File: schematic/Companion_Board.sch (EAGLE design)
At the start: 43 parts, among them J10 QSH-030-01-X-D-A, Q1 CSM-7X-DU

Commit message: Updated spec and schematic with pinheaders for reset and power.
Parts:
- added JP11: (no value), pinhead:PINHD-1X4/90
- added R12, R13: NC, resistor:R-US_R0805
- added TP4: TPPAD1-13, testpad:TPPAD1-13
- R7, R9: value ??k -> 270
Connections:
- net N$25 renamed FORCE_RESET
- net SBW_RST renamed SBW_TDIO
- removed net N$54: U$1.P1.4/UCA0STE/TCK/OA0+/A4
- removed net N$55: U$1.P1.5/UCA0CLK/TMS/TRI0O/A5
- new net N$25: R12.1, U$1.P1.4/UCA0STE/TCK/OA0+/A4
- new net N$34: R13.1, U$1.P1.5/UCA0CLK/TMS/TRI0O/A5
- new net N$48: J10.40, JP7.9
- net +3V3: now also TP4.TP
- net BSL_RXD: now also U$1.P1.7/UCA-TXD/UCA0SIMO/TB0.2/TDO/TRI0+/A7/VREF+; no longer U$1.P1.6/UCA0RXD/UCA0SOMI/TB0.1/TDI/TCLK/TRI0-/A6
- net BSL_TXD: now also U$1.P1.6/UCA0RXD/UCA0SOMI/TB0.1/TDI/TCLK/TRI0-/A6; no longer U$1.P1.7/UCA-TXD/UCA0SIMO/TB0.2/TDO/TRI0+/A7/VREF+
- net GND: now also JP11.2, JP11.4, R12.2, R13.2, TP1.TP
- net POWER_BTN_R: now also JP11.3
- net RESET_IN_R_L: now also JP11.1; no longer J10.40, JP7.9
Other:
- note added: "1-2: Board is internally powered (by Jetson), VCC_TARGET provides board voltage to debugger. 2-3: Board is powered by debugger."
- note added: "Grounding ADR sets I2C addr to 0x76 Connecting CS to VDDIO at power-up enables I2C interface."
- note added: "J10: Debug Connector Not populated"
- note added: "Reset_Switch Gnd Power_Switch Gnd"
- note added: "This is RXD/TXD from the perspective of the debugger."
- note removed: "Grounding ADR sets I2C addr to 0x76"
- note removed: "J10: Debug Connector"
- moved on the sheet: J10, JP6, JP7

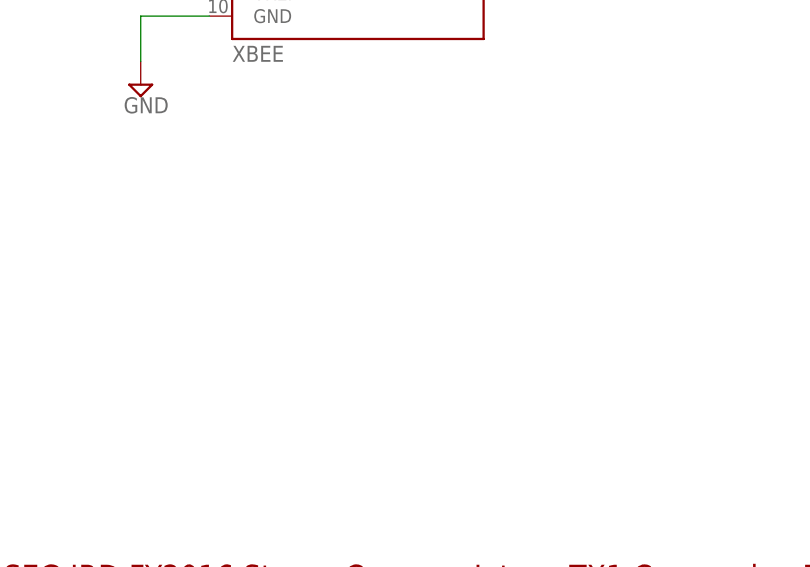
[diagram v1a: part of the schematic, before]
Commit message: Added mounting holes.
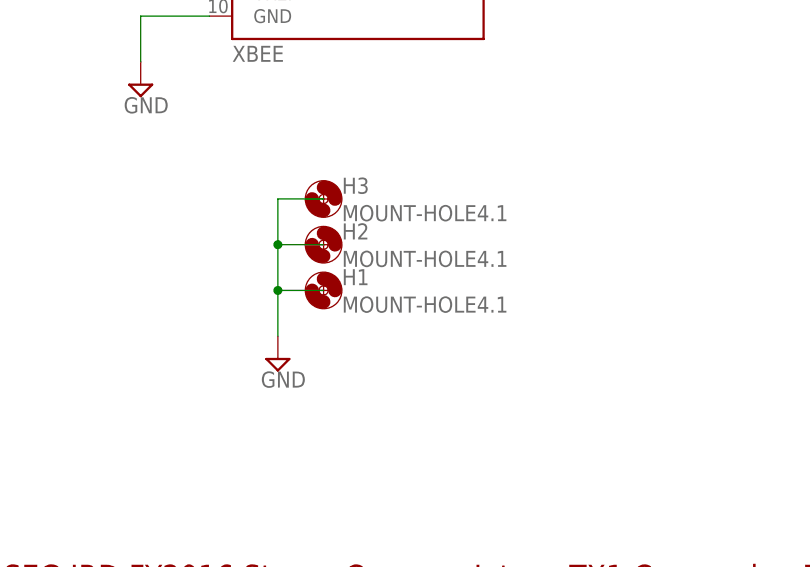
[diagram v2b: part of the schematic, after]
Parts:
- added H1, H2, H3: MOUNT-HOLE4.1, holes:MOUNT-HOLE4.1
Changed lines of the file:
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@@
 <part name="JP11" library="pinhead" deviceset="PINHD-1X4" device="/90"/>
 <part name="SUPPLY22" library="supply2" deviceset="GND" device=""/>
+<part name="H1" library="holes" deviceset="MOUNT-HOLE" device="4.1"/>
+<part name="H2" library="holes" deviceset="MOUNT-HOLE" device="4.1"/>
+<part name="H3" library="holes" deviceset="MOUNT-HOLE" device="4.1"/>
+<part name="SUPPLY23" library="supply2" deviceset="GND" device=""/>
 </parts>
 <sheets>
@@
 <instance part="JP11" gate="A" x="170.18" y="-7.62"/>
 <instance part="SUPPLY22" gate="GND" x="154.94" y="-17.78"/>
+<instance part="H1" gate="G$1" x="381" y="2.54"/>
+<instance part="H2" gate="G$1" x="381" y="7.62"/>
+<instance part="H3" gate="G$1" x="381" y="12.7"/>
+<instance part="SUPPLY23" gate="GND" x="375.92" y="-5.08"/>
 </instances>
 <busses>
@@
 <junction x="154.94" y="-10.16"/>
 </segment>
+<segment>
+<pinref part="SUPPLY23" gate="GND" pin="GND"/>
+<wire x1="375.92" y1="-2.54" x2="375.92" y2="2.54" width="0.1524" layer="91"/>
+<wire x1="381" y1="2.54" x2="375.92" y2="2.54" width="0.1524" layer="91"/>
+<wire x1="375.92" y1="2.54" x2="375.92" y2="7.62" width="0.1524" layer="91"/>
+<junction x="375.92" y="2.54"/>
+<wire x1="381" y1="7.62" x2="375.92" y2="7.62" width="0.1524" layer="91"/>
+<wire x1="375.92" y1="7.62" x2="375.92" y2="12.7" width="0.1524" layer="91"/>
+<wire x1="375.92" y1="12.7" x2="381" y2="12.7" width="0.1524" layer="91"/>
+<junction x="375.92" y="7.62"/>
+</segment>
 </net>

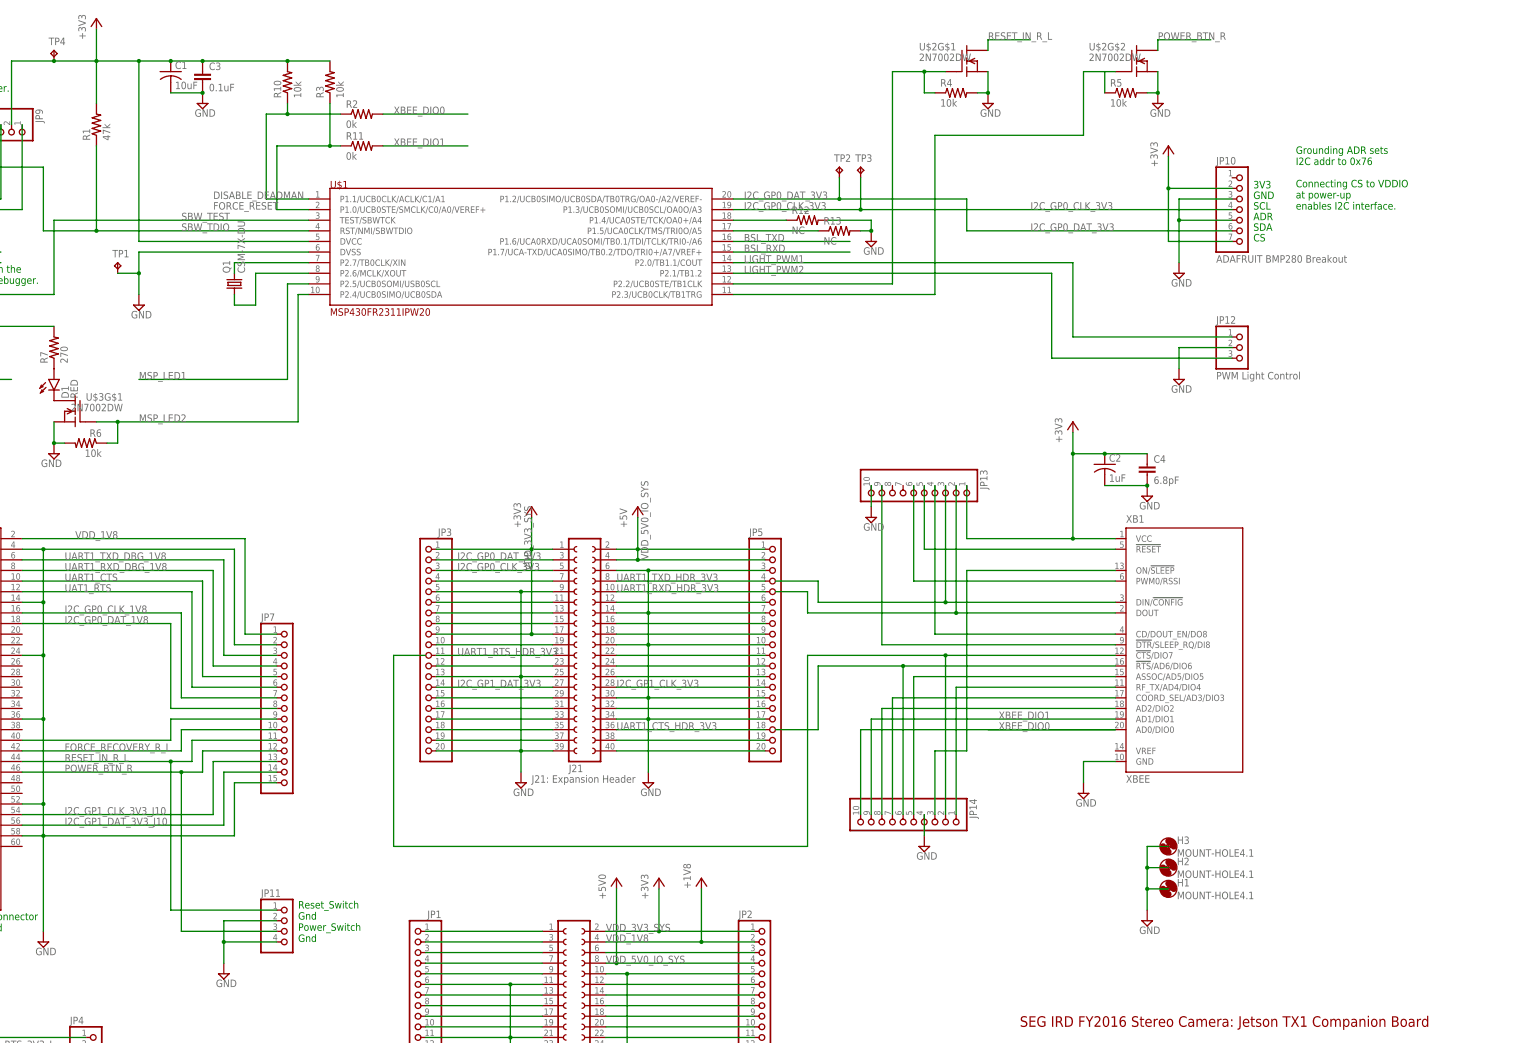
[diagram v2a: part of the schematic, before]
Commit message: Working on companion board layout.
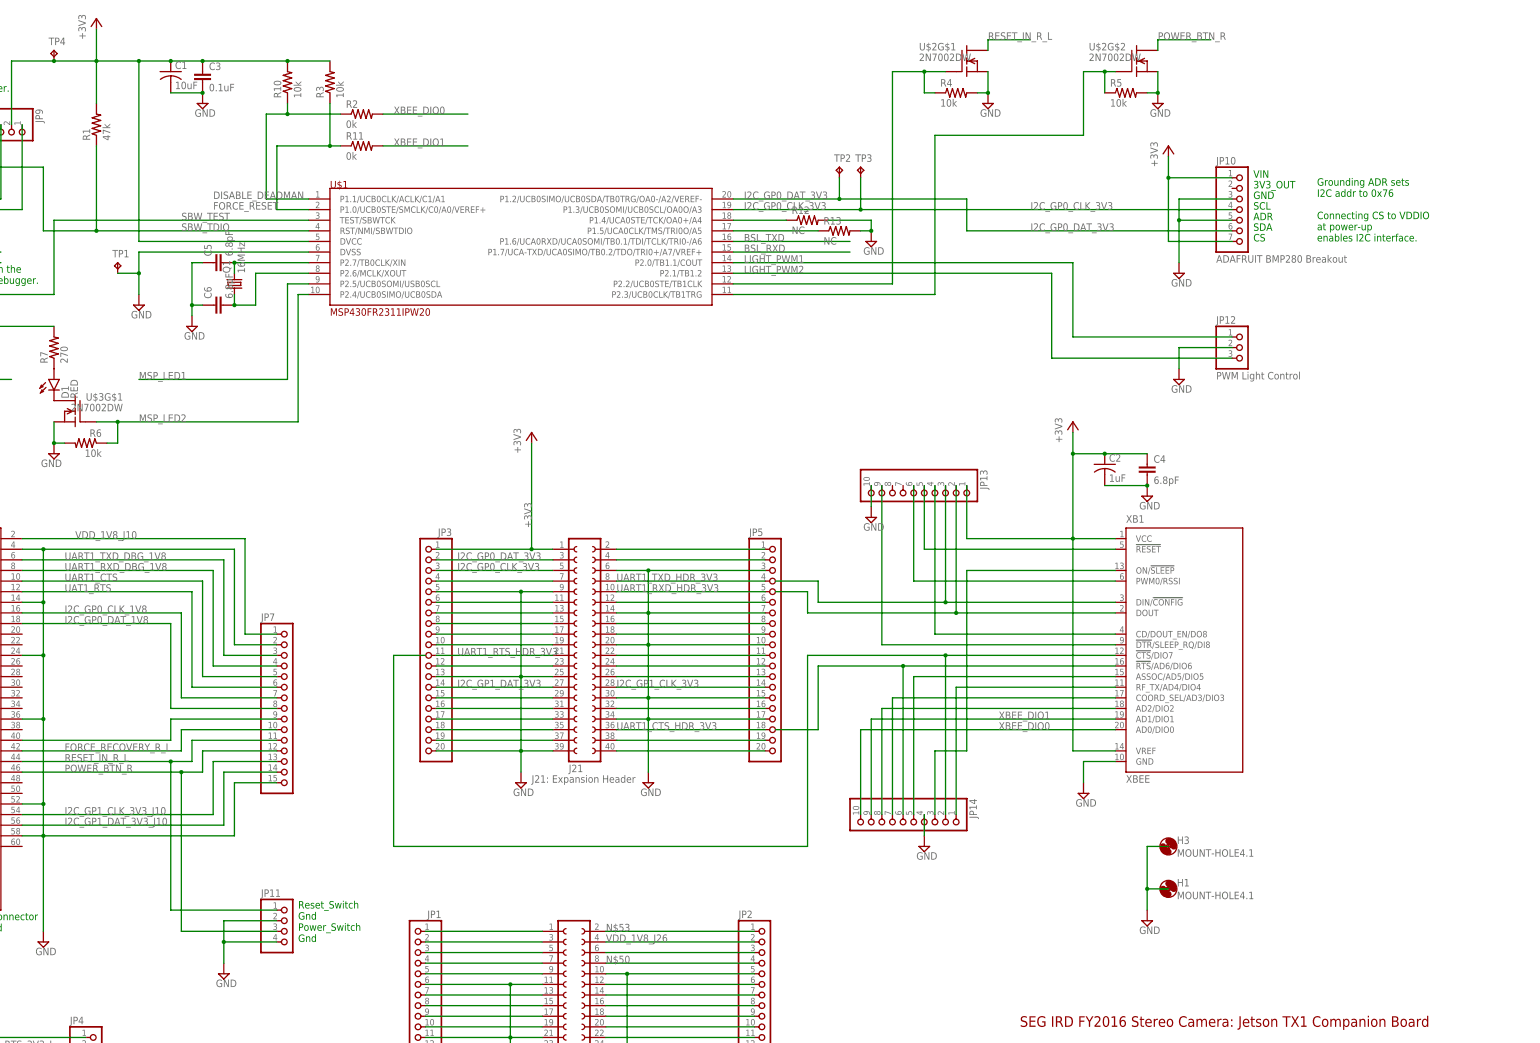
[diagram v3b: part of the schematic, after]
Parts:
- removed H2: MOUNT-HOLE4.1, holes:MOUNT-HOLE4.1
- added C5, C6: 6.8pF, resistor:C-EUC0805
- JP10: device pinhead:PINHD-1X7 -> companion_board:ADAFRUIT_BMP280_BREAKOUT
- Q1: value CSM-7X-DU -> 16MHz; device crystal:CSM-7X-DU -> crystal:CRYSTALHC49UP
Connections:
- net +5V renamed N$54
- removed net VDD_3V3_SYS: J21.1, J21.17, JP3.1, JP3.9
- new net N$50: J21.4, JP5.2
- new net N$53: J21.17, JP3.9
- new net N$55: J26.2, JP2.1
- new net VDD_1V8_J10: J10.2, JP7.1
- new net VDD_1V8_J26: J26.4, JP2.2
- net +3V3: now also J21.1, JP10.1, JP3.1, XB1.VREF; no longer J26.2, JP10.2, JP2.1
- net GND: now also C5.1, C6.1
- net N$41: now also C5.2
- net N$47: now also C6.2
- net VDD_1V8: no longer J10.2, J26.4, JP2.2, JP7.1
- net VDD_5V0_IO_SYS: no longer J21.4, JP5.2
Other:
- note added: "3V3_OUT"
- note added: "VIN"
- note removed: "3V3"

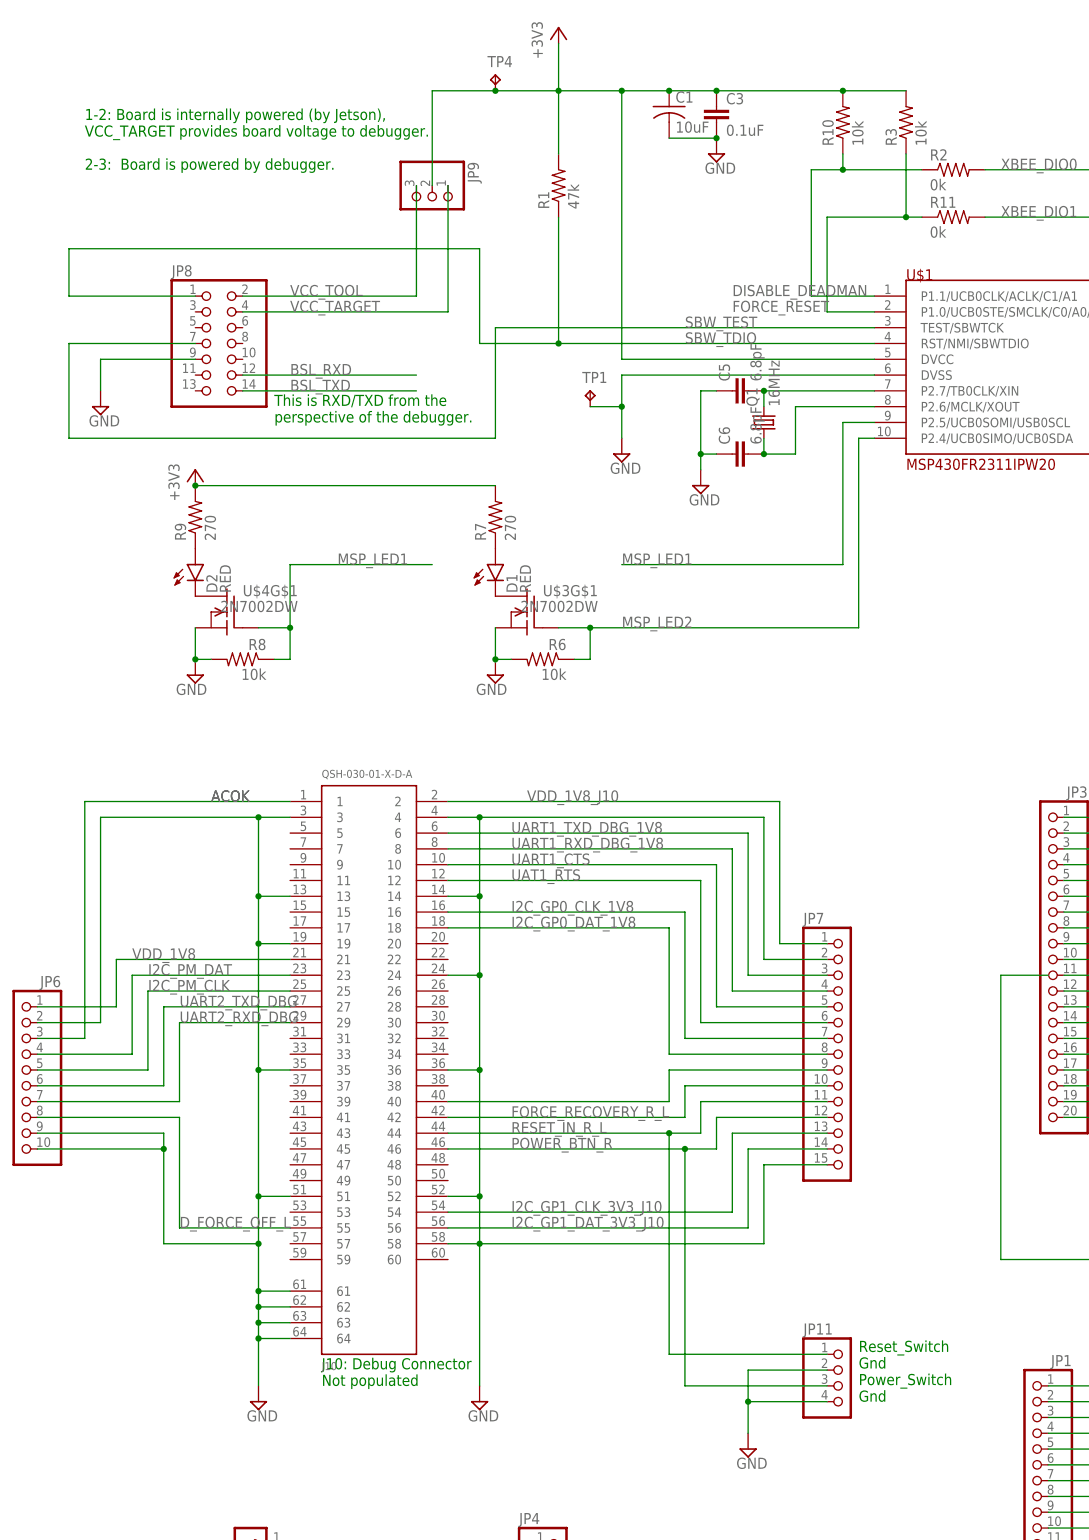
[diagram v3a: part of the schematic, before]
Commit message: Removed debug connector, now have parts laid out.
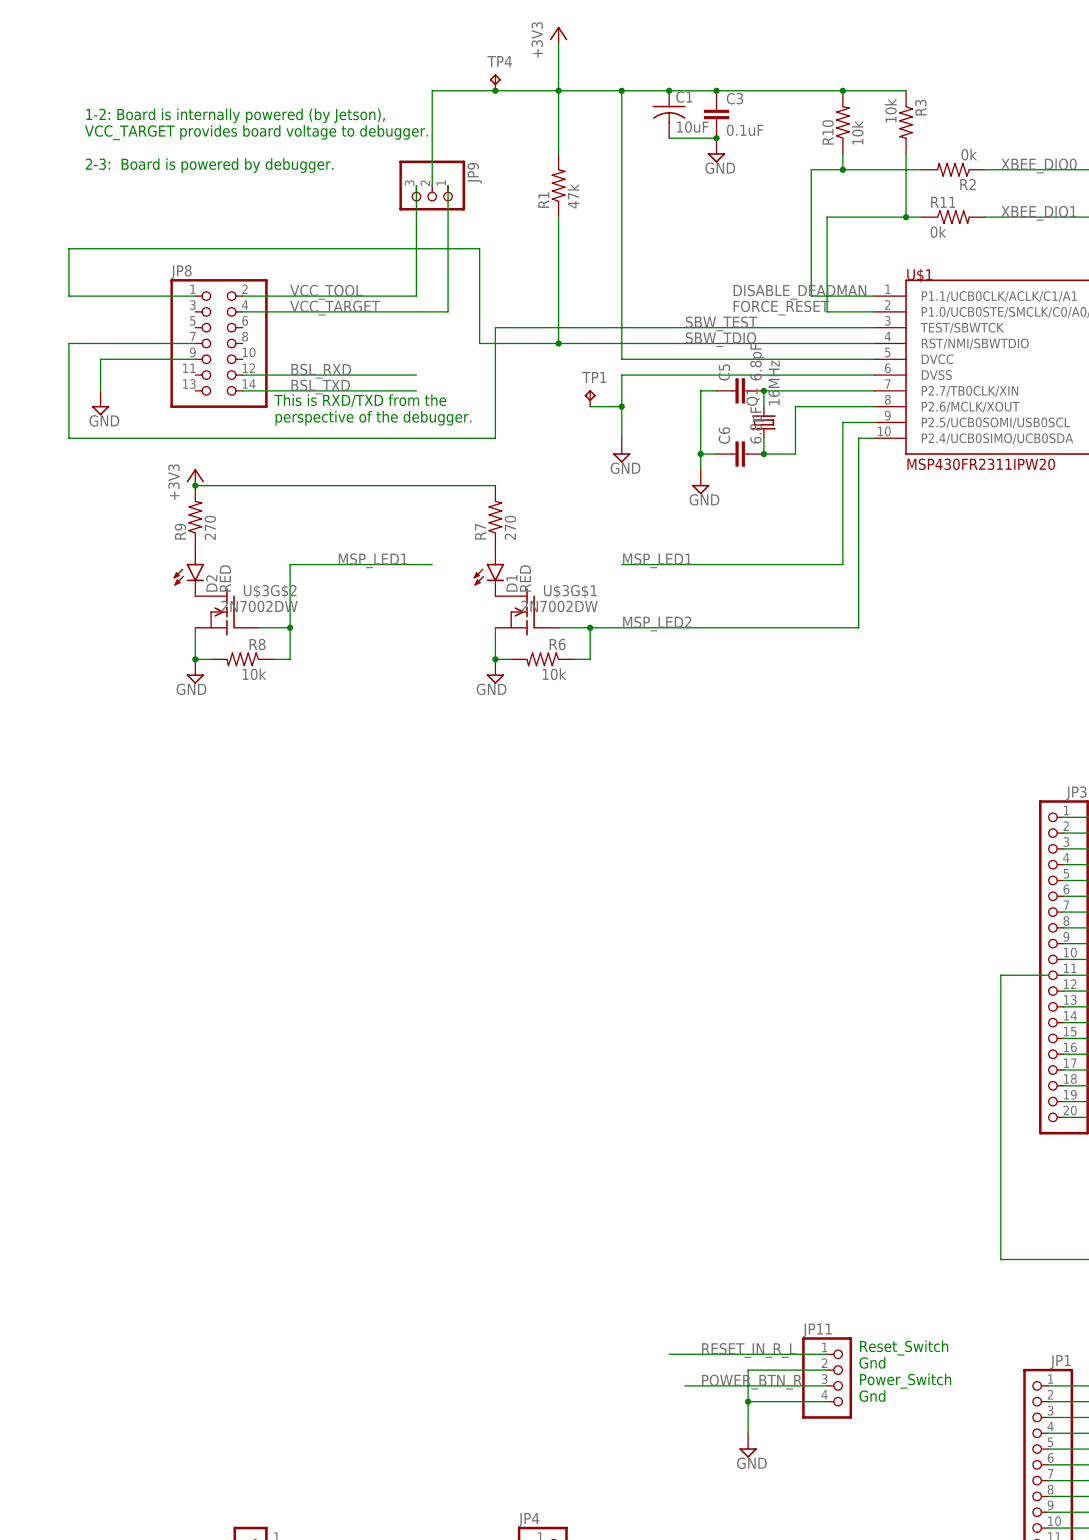
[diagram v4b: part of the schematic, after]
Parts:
- removed J10: QSH-030-01-X-D-A, QSH-030-01-X-D-A:QSH-030-01-X-D-A
- removed JP6: (no value), pinhead:PINHD-1X10
- removed JP7: (no value), pinhead:PINHD-1X15
- removed U$4: 2N7002DW, companion_board:2N7002DW
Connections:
- removed net ACOK: J10.1, JP6.3
- removed net D_FORCE_OFF_L: J10.55, JP6.8
- removed net FORCE_RECOVERY_R_L: J10.42, JP7.10
- removed net I2C_GP0_CLK_1V8: J10.16, JP7.7
- removed net I2C_GP0_DAT_1V8: J10.18, JP7.8
- removed net I2C_GP1_CLK_3V3_J10: J10.54, JP7.13
- removed net I2C_GP1_DAT_3V3_J10: J10.56, JP7.14
- removed net I2C_PM_CLK: J10.25, JP6.5
- removed net I2C_PM_DAT: J10.23, JP6.4
- removed net N$48 (its old number): J10.40, JP7.9
- removed net N$72: D2.C, U$4G$1.D
- removed net UART1_CTS: J10.10, JP7.5
- removed net UART1_RXD_DBG_1V8: J10.8, JP7.4
- removed net UART1_TXD_DBG_1V8: J10.6, JP7.3
- removed net UART2_RXD_DBG: J10.29, JP6.7
- removed net UART2_TXD_DBG: J10.27, JP6.6
- removed net UAT1_RTS: J10.12, JP7.6
- removed net VDD_1V8: J10.21, JP6.1
- removed net VDD_1V8_J10: J10.2, JP7.1
- new net N$58: D2.C, U$3G$2.D
- net +3V3: now also R3.1; no longer R3.2
- net DISABLE_DEADMAN: now also R2.2; no longer R2.1
- net FORCE_RESET: now also R3.2; no longer R3.1
- net GND: now also U$3G$2.S; no longer J10.13, J10.14, J10.19, J10.24, J10.3, J10.35, J10.36, J10.4, J10.51, J10.52, J10.58, J10.61, J10.62, J10.63, J10.64, JP6.10, JP6.2, JP6.9, JP7.15, JP7.2, U$4G$1.S
- net MSP_LED1: now also U$3G$2.G; no longer U$4G$1.G
- net POWER_BTN_R: no longer J10.46, JP7.12
- net RESET_IN_R_L: no longer J10.44, JP7.11
- net XBEE_DIO0: now also R2.1; no longer R2.2
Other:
- note removed: "J10: Debug Connector Not populated"
- moved on the sheet: R2, R3
